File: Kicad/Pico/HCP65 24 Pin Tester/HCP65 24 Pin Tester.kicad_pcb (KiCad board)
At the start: 2 copper layers, 92 x 81.8 mm, 75 parts, among them IC1 SN74ABT245BDBR, IC2 SN74ABT245BDBR, IC3 SN74ABT245BDBR, J1 6339167-2, J3 Conn_01x12_Socket, J8 Conn_01x12_Socket, J9 Conn_01x12_Socket

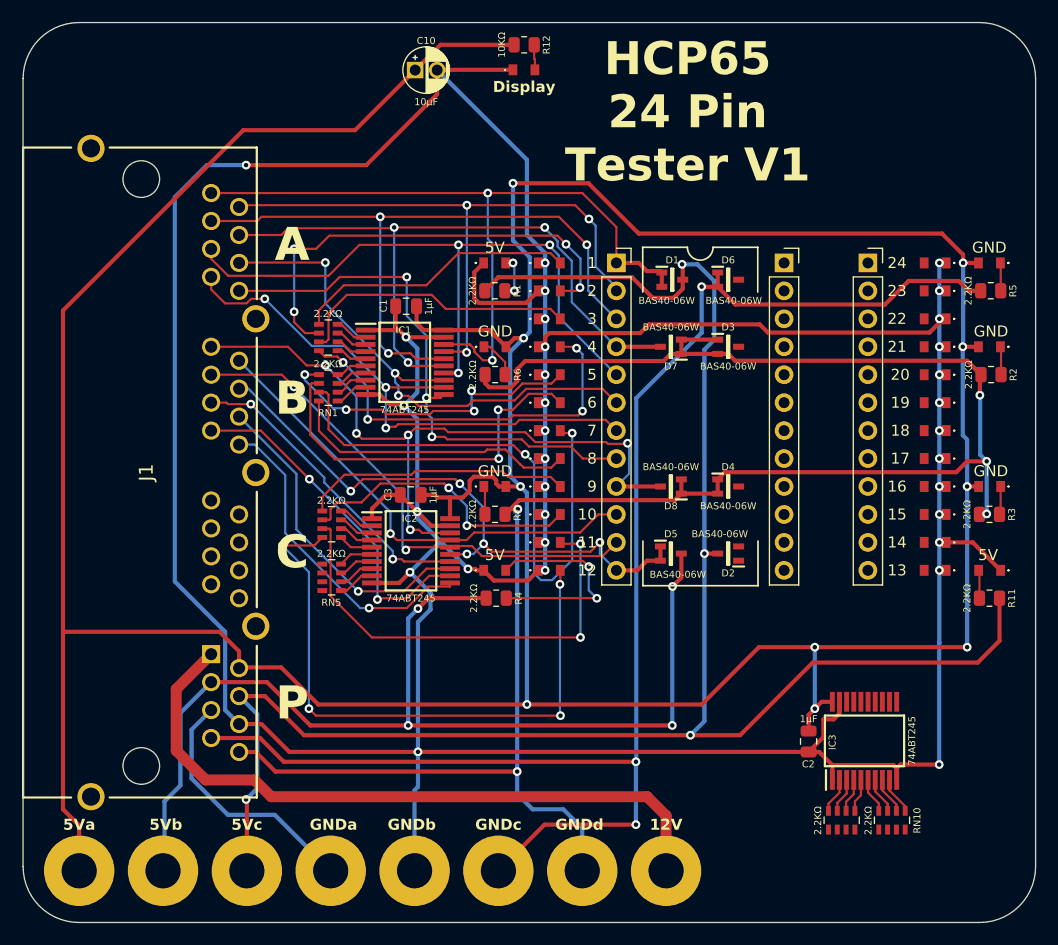
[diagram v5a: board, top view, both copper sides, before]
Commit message: Fixed 24pin Tester board.
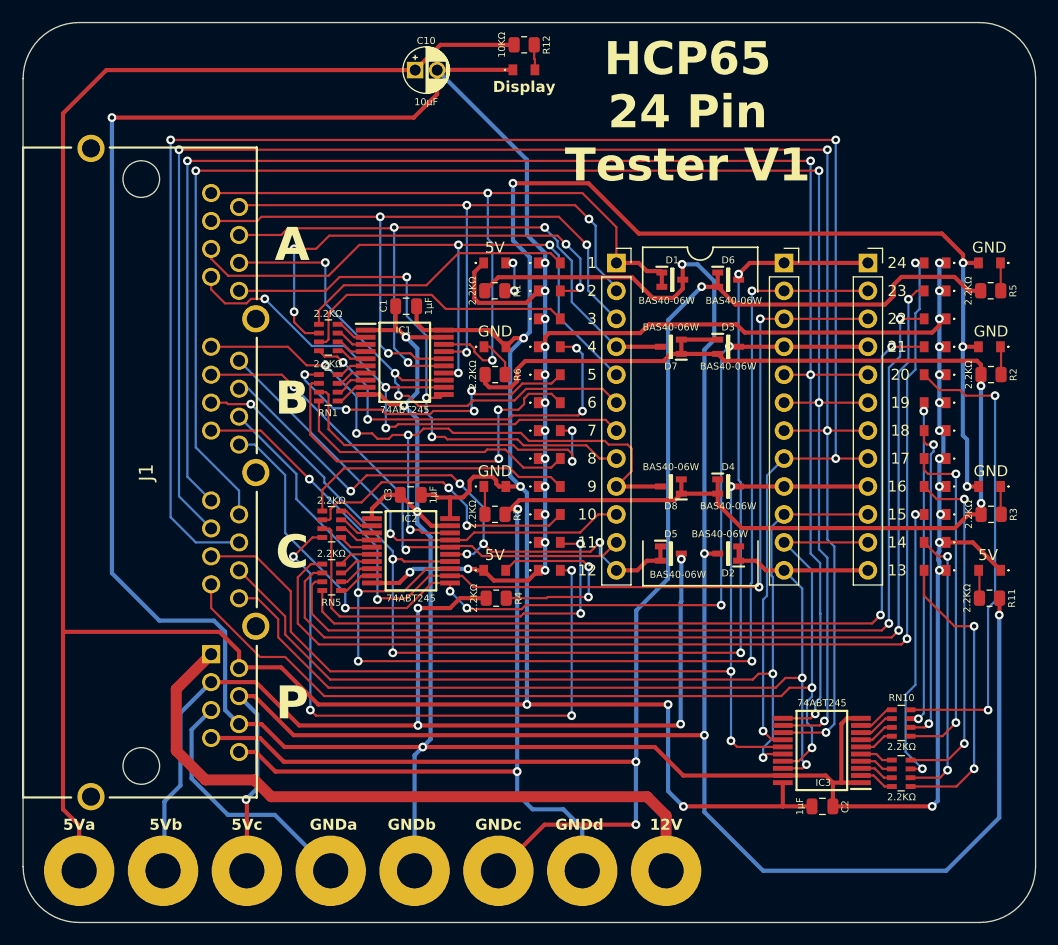
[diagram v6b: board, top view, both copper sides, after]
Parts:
- moved RN10 8.91 mm to (62.7, 48.2), turned to 180 degrees
- moved RN9 6.93 mm to (62.7, 52.7), turned to 180 degrees
- moved C2 6.04 mm to (55.5, 55.7), turned to -90 degrees
- moved IC3 3.97 mm to (55.5, 50.7), turned to 180 degrees
- moved R3 0.15 mm to (70.9, 29.2)
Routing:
- net /IO19: track 0.00 -> 166.2 mm, vias 0 -> 4
- net /IO18: track 0.00 -> 159.6 mm, vias 0 -> 4
- net /IO17: track 0.00 -> 151.5 mm, vias 0 -> 4
- net /IO16: track 0.00 -> 150.0 mm, vias 0 -> 4
- net /S12: track 0.00 -> 98.9 mm, vias 0 -> 2
- net /IO20: track 0.00 -> 94.2 mm, vias 0 -> 3
- net /S13: track 0.00 -> 92.4 mm, vias 0 -> 2
- net /IO22: track 0.00 -> 91.3 mm, vias 0 -> 2
- net /IO23: track 0.00 -> 90.1 mm, vias 0 -> 2
- net /S14: track 0.00 -> 87.3 mm, vias 0 -> 2
- net /IO12: track 28.4 -> 115.7 mm, vias 2 -> 5
- net /IO13: track 29.6 -> 116.0 mm, vias 1 -> 4
- net /IO21: track 0.00 -> 86.4 mm, vias 0 -> 2
- net /S15: track 0.00 -> 81.2 mm, vias 0 -> 2
- net /IO15: track 29.6 -> 92.8 mm, vias 1 -> 5
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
